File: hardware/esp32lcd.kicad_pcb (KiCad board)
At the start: 2 copper layers, 78 x 44 mm, 25 parts, among them J1 Conn_02x05_Odd_Even, J11 USB_B_Micro, J12 Barrel_Jack_Switch, Q1 MMBT5551, Q12 MMBT5551, Q13 MMBT5401, U11 SRV05-4, U12 CH340C, U13 AMS1117-3.3, U14 ESP32-WROOM-32D, U15 ILI9341_SPI_Touch_SD

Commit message: Last version before moving to Kicad10 and JLC Basic/Extended libraries
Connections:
- net /RXD0 renamed RXD0
- net /TXD0 renamed TXD0
- net Net-(Q1-Pad3) renamed LOAD
- net Net-(U14-Pad27) renamed RXD2
- net Net-(U14-Pad28) renamed TXD2
- Q13 pad 3: BACKLIGHT -> LCDLED
- R15 pad 1: Net-(R15-Pad1) -> BACKLIGHT
- U14 pad 11: Net-(R15-Pad1) -> BACKLIGHT
- U15 pad 8: BACKLIGHT -> LCDLED
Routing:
- net LCDLED: track 0.00 -> 17.7 mm, vias 0 -> 1
- net Net-(R15-Pad1): track 9.68 -> 0.00 mm
- net BACKLIGHT: track 17.7 -> 9.68 mm, vias 1 -> 0

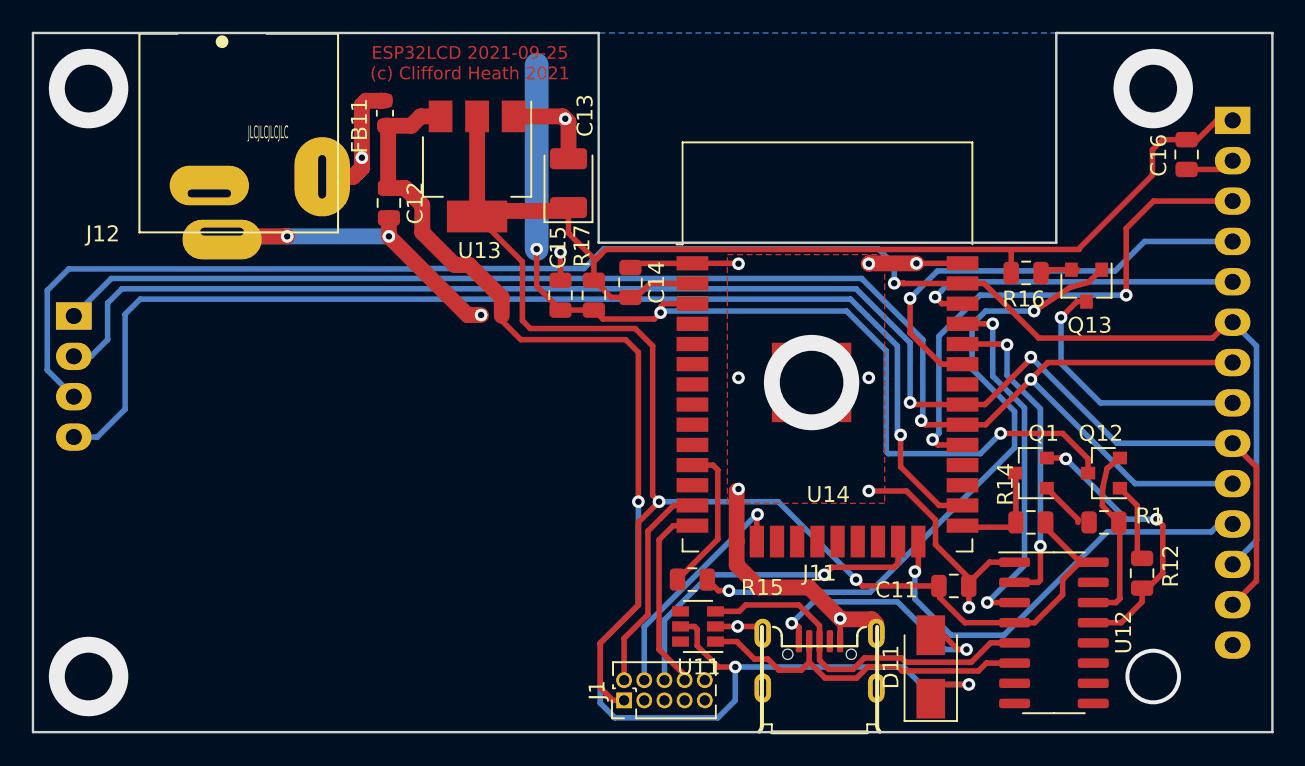
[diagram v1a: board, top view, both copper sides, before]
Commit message: Moved to Kicad 10 and JLC Basic/Extended parts where possible
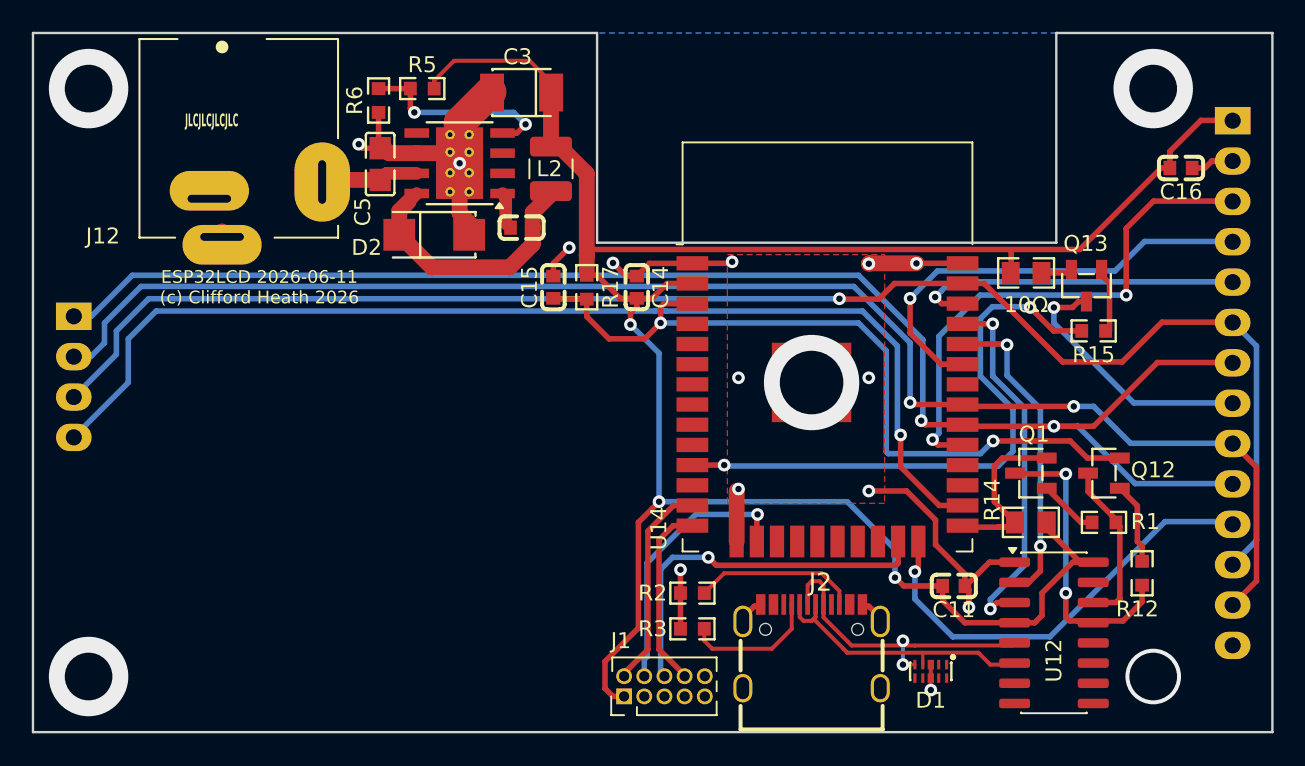
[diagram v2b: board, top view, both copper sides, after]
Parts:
- removed C12: 100n, Capacitor_SMD:C_0805_2012Metric
- removed C13: 100uF, cjh_jlcpcb:CP_EIA-3528-21_Kemet-B
- removed D11: SS14, Diode_SMD:D_SMA
- removed FB11: BLM18PG121SN1D, Inductor_SMD:L_0603_1608Metric
- removed J11: USB_B_Micro, cjh_jlcpcb:XKB_Micro_USB_B_U254
- removed U11: SRV05-4, cjh_jlcpcb:SOT-23-6R
- removed U13: AMS1117-3.3, cjh_jlcpcb:SOT-223-3_TabPin2
- added C3: 100uF, jlcbasic:CASE-B_3528, F.Cu at (105.8, 114.8)
- added C4: 10nF, jlcbasic:C0603, F.Cu at (105.8, 123.2)
- added C5: 4.7uF, jlcbasic:C0805, F.Cu at (96.8, 119.2)
- added D1: TPAZ1143-04F, cjh_jlcpcb:DFN-10_L2.5-W1.0-P0.50-BL-A, F.Cu at (131.5, 151.2)
- added D2: SS34, jlcbasic:SMA_L4.3-W2.6-LS5.2-RD, F.Cu at (100.2, 123.7)
- added J2: USB_C_Receptacle_USB2.0_14P, cjh_jlcpcb:USB-C_SMD-TYPE-C-31-M-12, F.Cu at (124.0, 149.6)
- added L2: 15µH, Inductor_SMD:L_1210_3225Metric, F.Cu at (107.6, 119.5)
- added R2: 5.1kΩ, jlcbasic:R0603, F.Cu at (116.5, 146.2)
- added R3: 5.1kΩ, jlcbasic:R0603, F.Cu at (116.5, 148.5)
- added R5: 10kΩ, jlcbasic:R0603, F.Cu at (99.5, 114.5)
- added R6: 5.6kΩ, jlcbasic:R0603, F.Cu at (96.8, 115.2)
- added U3: TPS5430, Package_SO:TI_SO-PowerPAD-8_ThermalVias, F.Cu at (101.8, 119.2)
- C11, C14, C15, C16: value 100n -> 100nF; footprint Capacitor_SMD:C_0805_2012Metric -> jlcbasic:C0603
- Q1, Q12: value MMBT5551 -> MMBT2222A; footprint cjh_jlcpcb:SOT-23 -> jlcbasic:SOT-23-3_L2.9-W1.3-P1.90-LS2.4-BR
- Q13: footprint cjh_jlcpcb:SOT-23 -> jlcbasic:SOT-23-3_L2.9-W1.3-P1.90-LS2.4-BR
- R1, R12, R17: value 10k -> 10kΩ; footprint Resistor_SMD:R_0805_2012Metric -> jlcbasic:R0603
- R14: value 100k -> 100kΩ; footprint Resistor_SMD:R_0805_2012Metric -> jlcbasic:R0805
- R15: value 220R -> 220Ω; footprint Resistor_SMD:R_0805_2012Metric -> jlcbasic:R0603
- R16: value 10R -> 10Ω; footprint Resistor_SMD:R_0805_2012Metric -> jlcbasic:R0805_NEW
- U12: footprint cjh_jlcpcb:SOIC-16_3.9x9.9mm_P1.27mm -> Package_SO:SOIC-16_3.9x9.9mm_P1.27mm
- moved R15 29.7 mm to (141.8, 129.8), turned to 180 degrees
- moved C16 0.92 mm to (147.2, 119.5), turned to 180 degrees
- moved C15 0.67 mm to (107.8, 127.0), turned to -90 degrees
- moved R17 0.67 mm to (109.8, 127.0), turned to -90 degrees
- moved C14 0.50 mm to (113.0, 127.0), turned to -90 degrees
- moved J1 0.25 mm to (112.2, 152.8)
- moved J12 0.13 mm to (88.0, 117.4)
- turned C11 to 180 degrees
- turned R1 to 0 degrees
- turned R12 to -90 degrees
- turned R14 to 0 degrees
- turned R16 to 0 degrees
- turned U12 to 0 degrees
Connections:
- C11 pad 1: +3V3 -> GND
- C11 pad 2: GND -> +3V3
- C14 pad 1: +3V3 -> GND
- C14 pad 2: GND -> +3V3
- C15 pad 1: ESP_EN -> GND
- C15 pad 2: GND -> ESP_EN
- C16 pad 1: +3V3 -> GND
- C16 pad 2: GND -> +3V3
- J1 pad 10: Net-(J1-Pad10) -> unconnected-(J1-Pin_10-Pad10)
- J12 pad 2: Net-(FB11-Pad2) -> +SUPPLY
- J12 pad 3: Net-(J12-Pad3) -> unconnected-(J12-Pad3)
- Q1 pad 1: Net-(Q1-Pad1) -> Net-(Q1-B)
- Q1 pad 2: Net-(Q1-Pad2) -> LOAD
- Q1 pad 3: LOAD -> Net-(Q1-E)
- Q12 pad 1: Net-(Q12-Pad1) -> Net-(Q12-B)
- Q12 pad 2: Net-(Q12-Pad2) -> ESP_EN
- Q12 pad 3: ESP_EN -> Net-(Q12-E)
- Q13 pad 1: Net-(Q13-Pad1) -> Net-(Q13-B)
- Q13 pad 2: Net-(Q13-Pad2) -> Net-(Q13-E)
- R1 pad 1: Net-(Q12-Pad2) -> Net-(Q1-B)
- R1 pad 2: Net-(Q1-Pad1) -> Net-(Q12-E)
- R12 pad 1: Net-(Q1-Pad2) -> Net-(Q12-B)
- R12 pad 2: Net-(Q12-Pad1) -> Net-(Q1-E)
- R14 pad 1: +3V3 -> LOAD
- R14 pad 2: LOAD -> +3V3
- R15 pad 1: BACKLIGHT -> Net-(Q13-B)
- R15 pad 2: Net-(Q13-Pad1) -> BACKLIGHT
- R16 pad 1: Net-(Q13-Pad2) -> +3V3
- R16 pad 2: +3V3 -> Net-(Q13-E)
- R17 pad 1: ESP_EN -> +3V3
- R17 pad 2: +3V3 -> ESP_EN
- U12 pad 10: Net-(U12-Pad10) -> unconnected-(U12-~{DSR}-Pad10)
- U12 pad 11: Net-(U12-Pad11) -> unconnected-(U12-~{RI}-Pad11)
- U12 pad 12: Net-(U12-Pad12) -> unconnected-(U12-~{DCD}-Pad12)
- U12 pad 13: Net-(Q1-Pad2) -> Net-(Q1-E)
- U12 pad 14: Net-(Q12-Pad2) -> Net-(Q12-E)
- U12 pad 15: Net-(U12-Pad15) -> unconnected-(U12-R232-Pad15)
- U12 pad 7: Net-(U12-Pad7) -> unconnected-(U12-NC-Pad7)
- U12 pad 8: Net-(U12-Pad8) -> unconnected-(U12-NC-Pad8)
- U12 pad 9: Net-(U12-Pad9) -> unconnected-(U12-~{CTS}-Pad9)
- U14 pad 10: Net-(U14-Pad10) -> unconnected-(U14-IO25-Pad10)
- U14 pad 12: Net-(U14-Pad12) -> unconnected-(U14-IO27-Pad12)
- U14 pad 17: Net-(U14-Pad17) -> unconnected-(U14-SHD/SD2-Pad17)
- U14 pad 18: Net-(U14-Pad18) -> unconnected-(U14-SWP/SD3-Pad18)
- U14 pad 19: Net-(U14-Pad19) -> unconnected-(U14-SCS/CMD-Pad19)
- U14 pad 20: Net-(U14-Pad20) -> unconnected-(U14-SCK/CLK-Pad20)
- U14 pad 21: Net-(U14-Pad21) -> unconnected-(U14-SDO/SD0-Pad21)
- U14 pad 22: Net-(U14-Pad22) -> unconnected-(U14-SDI/SD1-Pad22)
- U14 pad 32: Net-(U14-Pad32) -> unconnected-(U14-NC-Pad32)
- U14 pad 4: Net-(U14-Pad4) -> unconnected-(U14-SENSOR_VP-Pad4)
- U14 pad 5: Net-(U14-Pad5) -> unconnected-(U14-SENSOR_VN-Pad5)
- U14 pad 6: Net-(U14-Pad6) -> unconnected-(U14-IO34-Pad6)
- U14 pad 7: Net-(U14-Pad7) -> unconnected-(U14-IO35-Pad7)
- U14 pad 8: Net-(U14-Pad8) -> unconnected-(U14-IO32-Pad8)
- U14 pad 9: Net-(U14-Pad9) -> unconnected-(U14-IO33-Pad9)
- U15 pad 14: Net-(U15-Pad14) -> unconnected-(U15-T_IRQ-Pad14)
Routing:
- net +5V: track 86.6 -> 0.00 mm, vias 3 -> 0
- net Net-(Q13-Pad1): track 41.6 -> 0.00 mm, vias 2 -> 0
- net BACKLIGHT: track 9.68 -> 36.9 mm, vias 0 -> 2
- net Net-(Q1-E): track 0.00 -> 19.9 mm, vias 0 -> 2
- net Net-(Q1-Pad2): track 18.2 -> 0.00 mm, vias 2 -> 0
- net GND: track 90.0 -> 71.8 mm, vias 20 -> 19
- net Net-(D11-Pad2): track 17.4 -> 0.00 mm, vias 2 -> 0
- net Net-(D2-K): track 0.00 -> 16.9 mm
- net Net-(U3-VSENSE): track 0.00 -> 12.6 mm, vias 0 -> 2
- net ESP_EN: track 61.3 -> 48.8 mm, vias 3 -> 2
- net Net-(FB11-Pad2): track 12.3 -> 0.00 mm, vias 1 -> 0
- net Net-(Q12-Pad2): track 11.5 -> 0.00 mm
- net Net-(Q12-E): track 0.00 -> 10.5 mm
- net Net-(J2-CC2): track 0.00 -> 10.2 mm
- net Net-(J2-CC1): track 0.00 -> 8.65 mm
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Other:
- outline, holes or cut-outs redrawn
- net class Default removed
- board text added: "ESP32LCD 2026-06-11 (c) Clifford Heath 2026"
- board text removed: "ESP32LCD 2021-09-25 (c) Clifford Heath 2021"
